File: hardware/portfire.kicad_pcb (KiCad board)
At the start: 2 copper layers, 100 x 100 mm, 199 parts, among them IC101 STM32F4xxVxTx, IC102 TPS62152, IC103 25AA02E48, IC104 ADP3335, IC105 SNx5176B, IC201 MAX5969x, IC202 KSZ8081RNA, IC203 MAX17503, IC301 TPS92512, J201 RJ45, J202 AUX POWER, P101 SWD_TC, P102 AUX_BUS_RX, P103 AUX_BUS_RX, P301 1, P302 2, P303 3, P304 4, P305 5, P306 6, P307 7, P308 8, P309 9, P310 10, P311 11, P312 12, P313 13, P314 14, P315 15, P316 16, P317 17, P318 18, P319 19, P320 20, P321 21, P322 22, P323 23, P324 24, P325 25, P326 26, P327 27, P328 28, P329 29, P330 30, Q301 NTR4501NT1G, Q302 NTR4501NT1G, Q303 NTR4501NT1G, Q304 NTR4501NT1G, Q305 NTR4501NT1G, Q306 NTR4501NT1G, Q307 NTR4501NT1G, Q308 NTR4501NT1G, Q309 NTR4501NT1G, Q310 NTR4501NT1G, Q311 NTR4501NT1G, Q312 NTR4501NT1G, Q313 NTR4501NT1G, Q314 NTR4501NT1G, Q315 NTR4501NT1G, Q316 NTR4501NT1G, Q317 NTR4501NT1G, Q318 NTR4501NT1G, Q319 NTR4501NT1G, Q320 NTR4501NT1G, Q321 NTR4501NT1G, Q322 NTR4501NT1G, Q323 NTR4501NT1G, Q324 NTR4501NT1G, Q325 NTR4501NT1G, Q326 NTR4501NT1G, Q327 NTR4501NT1G, Q328 NTR4501NT1G, Q329 NTR4501NT1G, Q330 NTR4501NT1G, T201 749010012A, X101 PART, X102 PART, X103 PART, X104 PART, Y201 25MHz

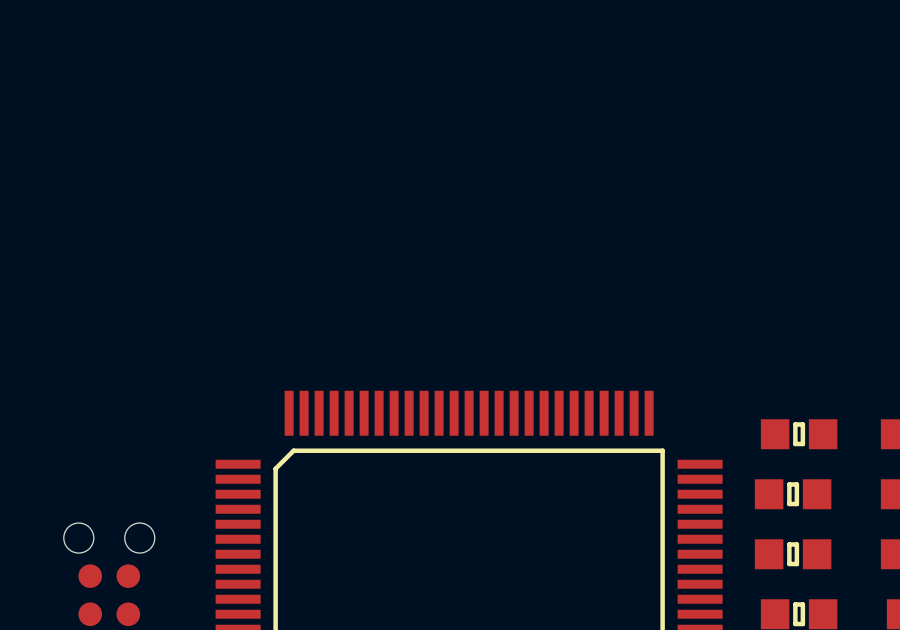
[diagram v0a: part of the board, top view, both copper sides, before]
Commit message: Added xtal to STM32
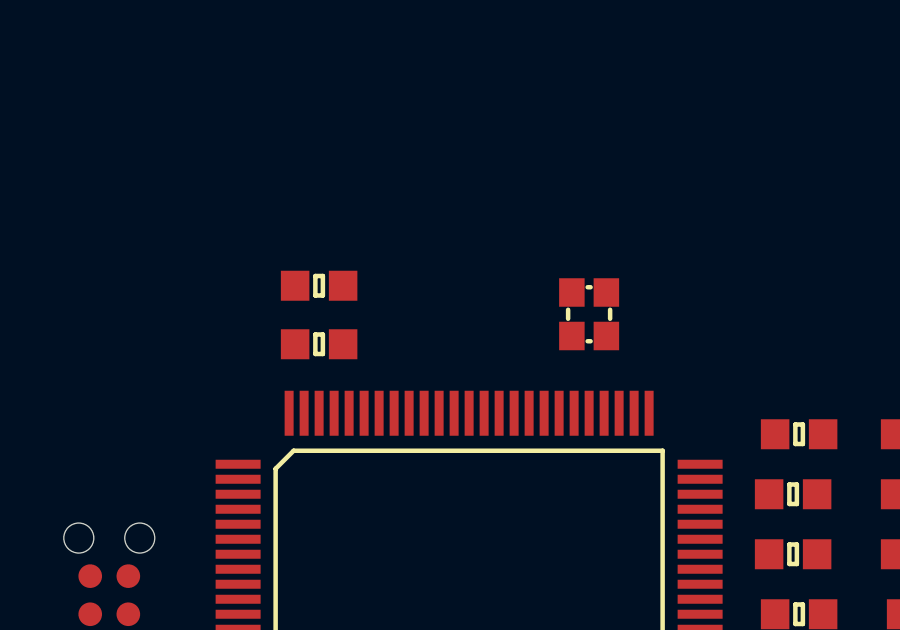
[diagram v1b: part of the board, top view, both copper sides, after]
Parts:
- added C122: 6pF, agg:0603, F.Cu at (218.0, 141.0)
- added C123: 6pF, agg:0603, F.Cu at (218.0, 139.1)
- added Y101: 26M, agg:XTAL-20x16, F.Cu at (227.0, 140.0)
- IC101: value STM32F4xxVxTx -> STM32F407VGT6TR
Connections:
- IC101 pad 12: (no net) -> Net-(C122-Pad1)
- IC101 pad 13: (no net) -> Net-(C123-Pad1)
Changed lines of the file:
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@@
 (kicad_pcb (version 4) (host pcbnew 4.0.4-stable)
   (general
-    (links 412)
-    (no_connects 383)
+    (links 420)
+    (no_connects 390)
     (area 19.949999 89.949999 120.050001 190.050001)
     (thickness 1.6)
@@
     (tracks 0)
     (zones 0)
-    (modules 199)
-    (nets 112)
+    (modules 202)
+    (nets 114)
   )
   (page A4)
@@
   (net 110 /SWDCLK)
   (net 111 "Net-(J201-Pad9)")
+  (net 112 "Net-(C122-Pad1)")
+  (net 113 "Net-(C123-Pad1)")
   (net_class Default "This is the default net class."
     (clearance 0.2)
@@
     (add_net "Net-(C103-Pad1)")
     (add_net "Net-(C116-Pad2)")
+    (add_net "Net-(C122-Pad1)")
+    (add_net "Net-(C123-Pad1)")
     (add_net "Net-(C201-Pad2)")
     (add_net "Net-(C202-Pad2)")
@@
       (effects (font (size 1 1) (thickness 0.15)))
     )
-    (fp_text value STM32F4xxVxTx (at 0 9.4) (layer F.Fab)
+    (fp_text value STM32F407VGT6TR (at 0 9.4) (layer F.Fab)
       (effects (font (size 1 1) (thickness 0.15)))
     )
@@
     (pad 11 smd rect (at -7.7 -1) (size 1.5 0.3) (layers F.Cu F.Paste F.Mask)
       (net 7 3v3))
-    (pad 12 smd rect (at -7.7 -0.5) (size 1.5 0.3) (layers F.Cu F.Paste F.Mask))
-    (pad 13 smd rect (at -7.7 0) (size 1.5 0.3) (layers F.Cu F.Paste F.Mask))
+    (pad 12 smd rect (at -7.7 -0.5) (size 1.5 0.3) (layers F.Cu F.Paste F.Mask)
+      (net 112 "Net-(C122-Pad1)"))
+    (pad 13 smd rect (at -7.7 0) (size 1.5 0.3) (layers F.Cu F.Paste F.Mask)
+      (net 113 "Net-(C123-Pad1)"))
     (pad 14 smd rect (at -7.7 0.5) (size 1.5 0.3) (layers F.Cu F.Paste F.Mask)
       (net 4 /nRST))
@@
     (pad "" np_thru_hole circle (at 1.8 1.8) (size 0.6 0.6) (drill 0.6) (layers *.Cu *.Mask F.SilkS))
   )
+  (module agg:0603 (layer F.Cu)
+    (at 218 141)
+    (fp_text reference C122 (at -2.225 0 90) (layer F.Fab)
+      (effects (font (size 1 1) (thickness 0.15)))
+    )
+    (fp_text value 6pF (at 2.225 0 90) (layer F.Fab)
+      (effects (font (size 1 1) (thickness 0.15)))
+    )
+    (fp_line (start -0.8 -0.4) (end 0.8 -0.4) (layer F.Fab) (width 0.01))
+    (fp_line (start 0.8 -0.4) (end 0.8 0.4) (layer F.Fab) (width 0.01))
+    (fp_line (start 0.8 0.4) (end -0.8 0.4) (layer F.Fab) (width 0.01))
+    (fp_line (start -0.8 0.4) (end -0.8 -0.4) (layer F.Fab) (width 0.01))
+    (fp_line (start -0.45 -0.4) (end -0.45 0.4) (layer F.Fab) (width 0.01))
+    (fp_line (start 0.45 -0.4) (end 0.45 0.4) (layer F.Fab) (width 0.01))
+    (fp_line (start -0.125 -0.325) (end 0.125 -0.325) (layer F.SilkS) (width 0.15))
+    (fp_line (start 0.125 -0.325) (end 0.125 0.325) (layer F.SilkS) (width 0.15))
+    (fp_line (start 0.125 0.325) (end -0.125 0.325) (layer F.SilkS) (width 0.15))
+    (fp_line (start -0.125 0.325) (end -0.125 -0.325) (layer F.SilkS) (width 0.15))
+    (fp_line (start -1.55 -0.75) (end 1.55 -0.75) (layer F.CrtYd) (width 0.01))
+    (fp_line (start 1.55 -0.75) (end 1.55 0.75) (layer F.CrtYd) (width 0.01))
+    (fp_line (start 1.55 0.75) (end -1.55 0.75) (layer F.CrtYd) (width 0.01))
+    (fp_line (start -1.55 0.75) (end -1.55 -0.75) (layer F.CrtYd) (width 0.01))
+    (pad 1 smd rect (at -0.8 0) (size 0.95 1) (layers F.Cu F.Paste F.Mask)
+      (net 112 "Net-(C122-Pad1)"))
+    (pad 2 smd rect (at 0.8 0) (size 0.95 1) (layers F.Cu F.Paste F.Mask)
+      (net 2 GND))
+    (model ${KISYS3DMOD}/Resistors_SMD.3dshapes/R_0603.wrl
+      (at (xyz 0 0 0))
+      (scale (xyz 1 1 1))
+      (rotate (xyz 0 0 0))
+    )
+  )
+  (module agg:0603 (layer F.Cu)
+    (at 218 139.050001)
+    (fp_text reference C123 (at -2.225 0 90) (layer F.Fab)
+      (effects (font (size 1 1) (thickness 0.15)))
+    )
+    (fp_text value 6pF (at 2.225 0 90) (layer F.Fab)
+      (effects (font (size 1 1) (thickness 0.15)))
+    )
+    (fp_line (start -0.8 -0.4) (end 0.8 -0.4) (layer F.Fab) (width 0.01))
+    (fp_line (start 0.8 -0.4) (end 0.8 0.4) (layer F.Fab) (width 0.01))
+    (fp_line (start 0.8 0.4) (end -0.8 0.4) (layer F.Fab) (width 0.01))
+    (fp_line (start -0.8 0.4) (end -0.8 -0.4) (layer F.Fab) (width 0.01))
+    (fp_line (start -0.45 -0.4) (end -0.45 0.4) (layer F.Fab) (width 0.01))
+    (fp_line (start 0.45 -0.4) (end 0.45 0.4) (layer F.Fab) (width 0.01))
+    (fp_line (start -0.125 -0.325) (end 0.125 -0.325) (layer F.SilkS) (width 0.15))
+    (fp_line (start 0.125 -0.325) (end 0.125 0.325) (layer F.SilkS) (width 0.15))
+    (fp_line (start 0.125 0.325) (end -0.125 0.325) (layer F.SilkS) (width 0.15))
+    (fp_line (start -0.125 0.325) (end -0.125 -0.325) (layer F.SilkS) (width 0.15))
+    (fp_line (start -1.55 -0.75) (end 1.55 -0.75) (layer F.CrtYd) (width 0.01))
+    (fp_line (start 1.55 -0.75) (end 1.55 0.75) (layer F.CrtYd) (width 0.01))
+    (fp_line (start 1.55 0.75) (end -1.55 0.75) (layer F.CrtYd) (width 0.01))
+    (fp_line (start -1.55 0.75) (end -1.55 -0.75) (layer F.CrtYd) (width 0.01))
+    (pad 1 smd rect (at -0.8 0) (size 0.95 1) (layers F.Cu F.Paste F.Mask)
+      (net 113 "Net-(C123-Pad1)"))
+    (pad 2 smd rect (at 0.8 0) (size 0.95 1) (layers F.Cu F.Paste F.Mask)
+      (net 2 GND))
+    (model ${KISYS3DMOD}/Resistors_SMD.3dshapes/R_0603.wrl
+      (at (xyz 0 0 0))
+      (scale (xyz 1 1 1))
+      (rotate (xyz 0 0 0))
+    )
+  )
+  (module agg:XTAL-20x16 (layer F.Cu)
+    (at 227 140)
+    (fp_text reference Y101 (at 0 -2.1) (layer F.Fab)
+      (effects (font (size 1 1) (thickness 0.15)))
+    )
+    (fp_text value 26M (at 0 2.2) (layer F.Fab)
+      (effects (font (size 1 1) (thickness 0.15)))
+    )
+    (fp_line (start -0.05 0.9) (end 0.05 0.9) (layer F.SilkS) (width 0.15))
+    (fp_line (start -0.7 -0.15) (end -0.7 0.15) (layer F.SilkS) (width 0.15))
+    (fp_line (start -0.05 -0.9) (end 0.05 -0.9) (layer F.SilkS) (width 0.15))
+    (fp_line (start 0.7 -0.15) (end 0.7 0.15) (layer F.SilkS) (width 0.15))
+    (fp_line (start -1.25 -1.45) (end 1.25 -1.45) (layer F.CrtYd) (width 0.01))
+    (fp_line (start -1.25 1.45) (end -1.25 -1.45) (layer F.CrtYd) (width 0.01))
+    (fp_line (start 1.25 1.45) (end -1.25 1.45) (layer F.CrtYd) (width 0.01))
+    (fp_line (start 1.25 -1.45) (end 1.25 1.45) (layer F.CrtYd) (width 0.01))
+    (fp_line (start 0.3 -0.4) (end 0.8 -0.4) (layer F.Fab) (width 0.01))
+    (fp_line (start 0.3 -1) (end 0.3 -0.4) (layer F.Fab) (width 0.01))
+    (fp_line (start -0.3 -0.4) (end -0.3 -1) (layer F.Fab) (width 0.01))
+    (fp_line (start -0.8 -0.4) (end -0.3 -0.4) (layer F.Fab) (width 0.01))
+    (fp_line (start -0.3 1) (end -0.3 0.4) (layer F.Fab) (width 0.01))
+    (fp_line (start -0.8 0.4) (end -0.3 0.4) (layer F.Fab) (width 0.01))
+    (fp_line (start 0.3 0.4) (end 0.3 1) (layer F.Fab) (width 0.01))
+    (fp_line (start 0.8 0.4) (end 0.3 0.4) (layer F.Fab) (width 0.01))
+    (fp_line (start 0.8 -1) (end 0.8 1) (layer F.Fab) (width 0.01))
+    (fp_line (start -0.8 -1) (end 0.8 -1) (layer F.Fab) (width 0.01))
+    (fp_line (start -0.8 1) (end -0.8 -1) (layer F.Fab) (width 0.01))
+    (fp_line (start 0.8 1) (end -0.8 1) (layer F.Fab) (width 0.01))
+    (pad 1 smd rect (at -0.575 -0.725 270) (size 0.95 0.85) (layers F.Cu F.Paste F.Mask)
+      (net 112 "Net-(C122-Pad1)"))
+    (pad 2 smd rect (at -0.575 0.725 270) (size 0.95 0.85) (layers F.Cu F.Paste F.Mask)
+      (net 2 GND))
+    (pad 3 smd rect (at 0.575 0.725 270) (size 0.95 0.85) (layers F.Cu F.Paste F.Mask)
+      (net 113 "Net-(C123-Pad1)"))
+    (pad 4 smd rect (at 0.575 -0.725 270) (size 0.95 0.85) (layers F.Cu F.Paste F.Mask)
+      (net 2 GND))
+  )
   (gr_line (start 120 90) (end 120 190) (angle 90) (layer Edge.Cuts) (width 0.1))

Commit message: Routed STM32 cruft and started on ethernet
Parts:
- moved P101 125.3 mm to (263.7, 36.3), turned to 180 degrees
- moved C103 116.1 mm to (263.4, 41.7)
- moved C107 115.6 mm to (241.3, 42.6), turned to 180 degrees
- moved C110 109.9 mm to (245.7, 36.7)
- moved IC101 108.6 mm to (252.3, 46.4)
- moved C112 108.2 mm to (263.4, 39.9)
- moved C104 107.4 mm to (241.3, 40.7), turned to 180 degrees
- moved C101 107.2 mm to (237.4, 48.9), turned to 180 degrees
- moved C109 104.4 mm to (241.3, 43.9), turned to 180 degrees
- moved C108 102.3 mm to (241.1, 49.9), turned to 180 degrees
- moved C106 97.5 mm to (241.1, 52.5), turned to 180 degrees
- moved C122 97.5 mm to (237.4, 45.5), turned to 180 degrees
- moved C111 96.6 mm to (259.7, 56.9), turned to 270 degrees
- moved C113 96.2 mm to (246.2, 56.1), turned to 180 degrees
- moved Y101 94.5 mm to (240.4, 46.5), turned to 315 degrees
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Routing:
- net GND: track 0.00 -> 55.8 mm, vias 0 -> 17
- net 3v3: track 0.00 -> 49.4 mm
- net /nRST: track 0.00 -> 34.2 mm, vias 0 -> 2
- net Net-(J201-Pad1): track 0.00 -> 28.4 mm
- net /ethernet/VB2: track 0.00 -> 26.2 mm, vias 0 -> 1
- net Net-(J201-Pad3): track 0.00 -> 23.2 mm
- net Net-(J201-Pad2): track 0.00 -> 22.6 mm
- net Net-(IC202-Pad6): track 0.00 -> 22.3 mm
- net /ethernet/VA1: track 0.00 -> 20.3 mm
- net Net-(IC202-Pad5): track 0.00 -> 18.9 mm
- net /ethernet/VB1: track 0.00 -> 15.6 mm, vias 0 -> 1
- net Net-(J201-Pad6): track 0.00 -> 14.8 mm
- net Net-(IC202-Pad4): track 0.00 -> 14.0 mm
- net /SWDIO: track 0.00 -> 10.3 mm
- net Net-(C213-Pad1): track 0.00 -> 9.60 mm
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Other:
- net class Default: via_dia 0.6 -> 0.8
- rule via_min_drill: 0.3 -> 0.4
- rule via_min_size: 0.4 -> 0.8

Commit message: various routing
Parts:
- removed TP203: 25MHz_XTAL, agg:TESTPAD
- moved R212 126.4 mm to (71.8, 73.3), turned to 270 degrees
- moved R211 125.1 mm to (73.2, 73.3), turned to 90 degrees
- moved JP201 114.9 mm to (80.5, 62.6)
- moved L203 113.7 mm to (73.5, 55.0), turned to 180 degrees
- moved R207 112.0 mm to (67.7, 69.6), turned to 270 degrees
- moved TP205 111.7 mm to (79.3, 62.6)
- moved IC203 109.5 mm to (71.2, 69.1)
- moved TP206 108.0 mm to (81.8, 62.6)
- moved C212 106.4 mm to (71.2, 63.4)
- moved C215 106.3 mm to (70.2, 73.3), turned to 270 degrees
- moved J202 106.3 mm to (82.2, 69.3), turned to 270 degrees
- moved C220 105.5 mm to (70.3, 65.8)
- moved C219 104.5 mm to (74.5, 69.2), turned to 90 degrees
- moved C222 101.6 mm to (76.0, 65.2), turned to 180 degrees
- moved C223 97.6 mm to (76.0, 62.9), turned to 180 degrees
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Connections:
- C217 pad 1: 3v3 -> Net-(C217-Pad1)
- C218 pad 1: 3v3 -> Net-(C217-Pad1)
- IC202 pad 2: Net-(IC202-Pad2) -> Net-(C217-Pad1)
- L202 pad 2: Net-(IC202-Pad2) -> Net-(C217-Pad1)
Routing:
- net GND: track 55.8 -> 127.5 mm, vias 17 -> 24
- net +6V: track 0.00 -> 31.6 mm
- net Net-(C222-Pad1): track 0.00 -> 29.6 mm
- net 3v3: track 49.4 -> 73.5 mm, vias 0 -> 2
- net /firing/RETURN: track 0.00 -> 23.6 mm
- net Net-(IC105-Pad7): track 0.00 -> 19.1 mm
- net Net-(IC105-Pad6): track 0.00 -> 18.6 mm
- net /firing/BUS: track 0.00 -> 16.2 mm
- net Net-(C304-Pad2): track 0.00 -> 12.8 mm
- net Net-(C220-Pad2): track 0.00 -> 9.33 mm
- net +48V: track 0.00 -> 9.05 mm
- net Net-(C217-Pad1): track 0.00 -> 7.12 mm
- net /firing/ARM: track 0.00 -> 6.11 mm, vias 0 -> 2
- net Net-(C221-Pad1): track 0.00 -> 6.00 mm
- net Net-(C302-Pad1): track 0.00 -> 4.28 mm
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
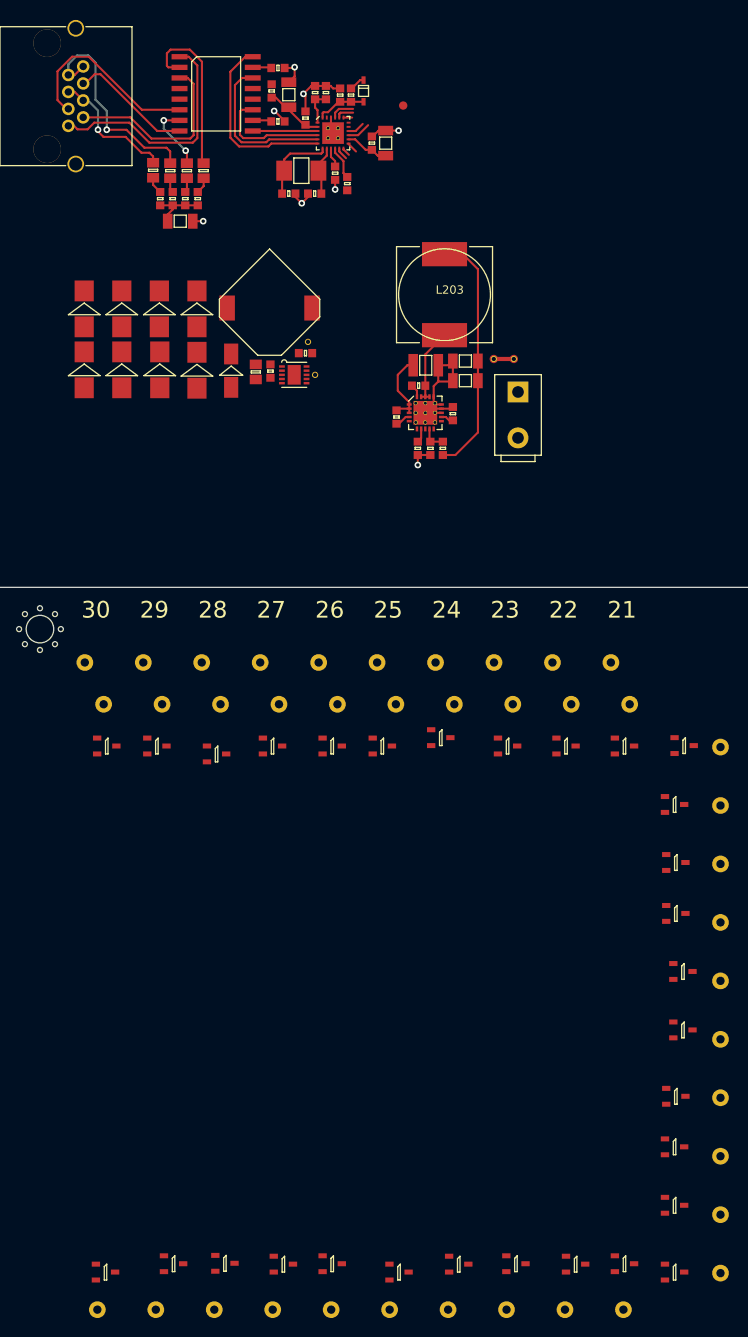
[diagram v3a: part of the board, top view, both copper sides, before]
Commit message: Invert ethernet magnetics ordering.
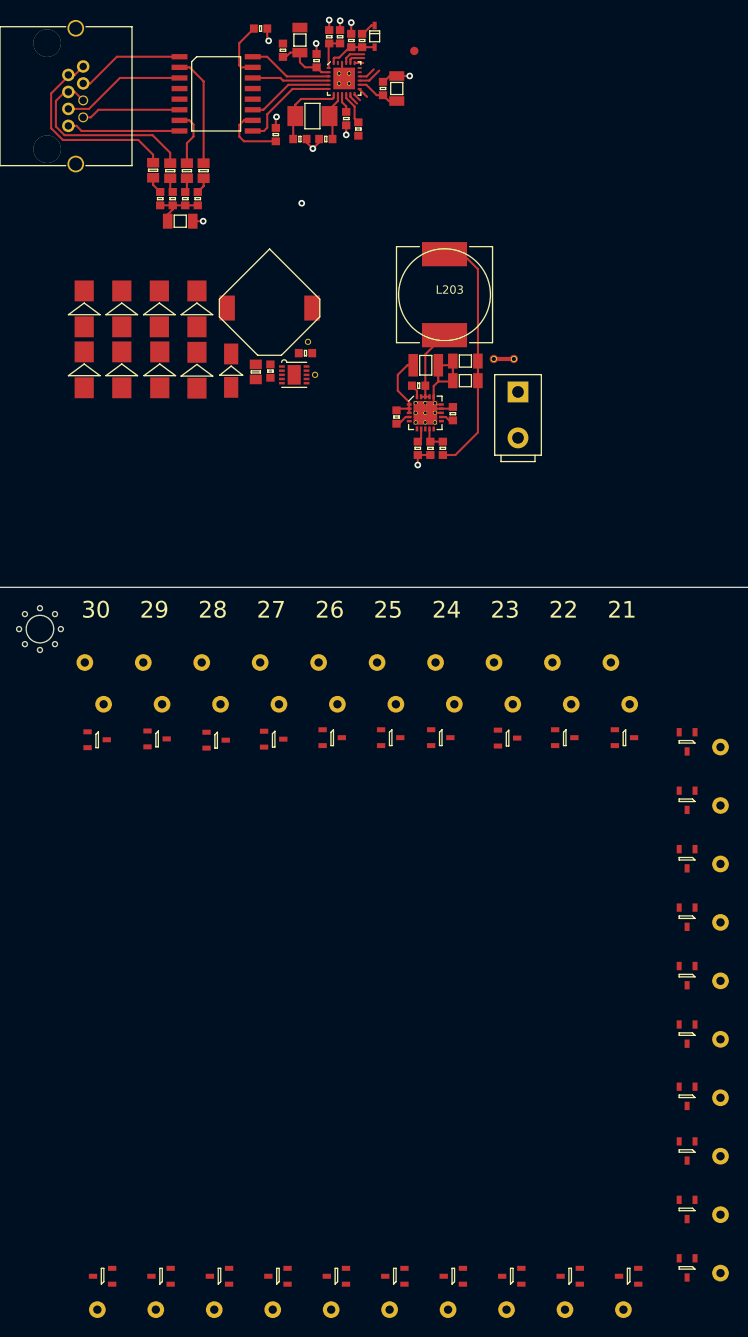
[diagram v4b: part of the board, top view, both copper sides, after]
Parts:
- moved C218 7.01 mm to (58.1, 26.9)
- moved C209 6.90 mm to (60.9, 24.1)
- moved C210 6.90 mm to (59.6, 24.1)
- moved IC202 6.67 mm to (61.4, 29.1)
- moved C213 6.67 mm to (56.1, 36.3)
- moved C217 6.67 mm to (56.1, 24.5)
- moved R209 6.67 mm to (63.1, 35.1)
- moved Y201 6.67 mm to (57.6, 33.6)
- moved C211 6.67 mm to (59.2, 36.3)
- moved C221 6.67 mm to (62.3, 24.5)
- moved D210 6.67 mm to (65.1, 24.0)
- moved R208 6.67 mm to (61.7, 33.9)
- moved R210 6.67 mm to (63.6, 24.5)
- moved C214 6.67 mm to (67.7, 30.3)
- moved C216 6.67 mm to (66.1, 30.3)
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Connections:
- C203 pad 2: GND -> Net-(C203-Pad2)
- J201 pad 4: /ethernet/VB1 -> /ethernet/VB2
- J201 pad 5: /ethernet/VB1 -> /ethernet/VB2
- J201 pad 7: /ethernet/VB2 -> /ethernet/VB1
- J201 pad 8: /ethernet/VB2 -> /ethernet/VB1
- J201 pad 9: Net-(J201-Pad9) -> Net-(C203-Pad2)
- T201 pad 1: Net-(J201-Pad1) -> Net-(J201-Pad6)
- T201 pad 11: Net-(IC202-Pad4) -> Net-(IC202-Pad5)
- T201 pad 14: Net-(IC202-Pad5) -> Net-(IC202-Pad4)
- T201 pad 16: Net-(IC202-Pad6) -> Net-(IC202-Pad3)
- T201 pad 3: Net-(J201-Pad2) -> Net-(J201-Pad3)
- T201 pad 6: Net-(J201-Pad3) -> Net-(J201-Pad2)
- T201 pad 8: Net-(J201-Pad6) -> Net-(J201-Pad1)
- T201 pad 9: Net-(IC202-Pad3) -> Net-(IC202-Pad6)
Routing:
- net Net-(J201-Pad1): track 28.4 -> 14.3 mm
- net Net-(J201-Pad2): track 22.6 -> 11.9 mm
- net Net-(IC202-Pad6): track 22.3 -> 12.1 mm
- net Net-(IC202-Pad5): track 18.9 -> 10.3 mm
- net /ethernet/VB1: track 15.6 -> 23.9 mm, vias 1 -> 0
- net Net-(J201-Pad3): track 23.2 -> 15.2 mm
- net /ethernet/VA1: track 20.3 -> 13.7 mm
- net GND: track 127.5 -> 121.9 mm, vias 24 -> 26
- net Net-(C207-Pad1): track 2.27 -> 7.83 mm
- net Net-(IC202-Pad4): track 14.0 -> 9.22 mm
- net Net-(C208-Pad1): track 2.25 -> 6.86 mm
- net /ethernet/VB2: track 26.2 -> 23.6 mm, vias 1 -> 0
- net Net-(IC202-Pad3): track 7.76 -> 10.1 mm
- net Net-(J201-Pad6): track 14.8 -> 13.1 mm
- net /ethernet/VA2: track 8.16 -> 6.83 mm, vias 2 -> 0
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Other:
- rule trace_min: 0.2 -> 0.15

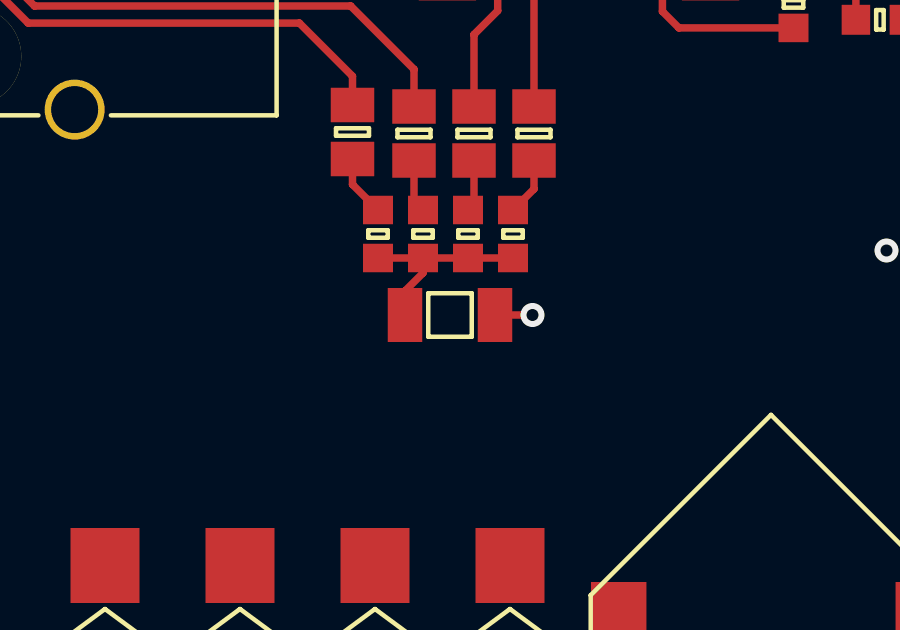
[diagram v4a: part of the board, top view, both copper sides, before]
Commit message: Removed pointless half of Bob Smith
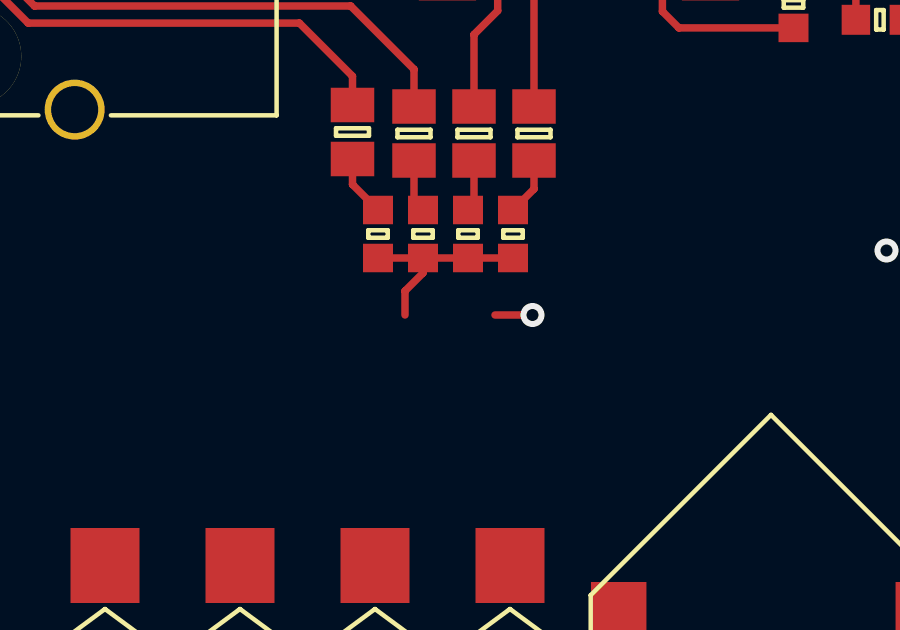
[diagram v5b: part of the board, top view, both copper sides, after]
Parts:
- removed C203: 1n 2kV, agg:1206
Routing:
- net Net-(J201-Pad9): track 1.25 -> 0.00 mm, vias 1 -> 0
- net (no net): track 0.00 -> 1.25 mm, vias 1 -> 2
